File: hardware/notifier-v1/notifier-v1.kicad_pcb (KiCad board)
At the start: 4 copper layers, 50 x 36 mm, 42 parts, among them J1 USB-C PWR/DATA, J2 GC9A01 DISPLAY, SW1 RESET, SW2 BOOT, SW3 BUTTON, U1 ESP32-S3-WROOM-1-N8R2, U2 USBLC6-2SC6, U3 TLV62569, U4 BME688, U5 SHT40-AD1B

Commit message: notifier-v1: USB 22 ohm series resistors, 1 uF at module 3V3, second buck output cap
Co-Authored-By: Claude Opus 5.5 <noreply@anthropic.com>
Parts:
- added C10: 1u, Capacitor_SMD:C_0402_1005Metric, F.Cu at (113.7, 110.6)
- added C11: 22u, Capacitor_SMD:C_0805_2012Metric, F.Cu at (130.2, 126.9)
- added R11: 22, Resistor_SMD:R_0402_1005Metric, F.Cu at (113.5, 116.5)
- added R12: 22, Resistor_SMD:R_0402_1005Metric, F.Cu at (113.5, 117.7)
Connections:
- U1 pad 13: /USB_DN -> /MCU/USB_DN_MCU
- U1 pad 14: /USB_DP -> /MCU/USB_DP_MCU
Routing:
- net /USB_DN: track 16.8 -> 32.9 mm, vias 2 -> 0
- net GND: track 178.0 -> 189.8 mm, vias 15 -> 18
- net /MCU/BTN: track 50.2 -> 42.8 mm, vias 9 -> 4
- net /MCU/BOOT: track 63.9 -> 69.6 mm, vias 4 -> 5
- net /MCU/USB_DN_MCU: track 0.00 -> 5.29 mm, vias 0 -> 2
- net /MCU/USB_DP_MCU: track 0.00 -> 3.89 mm, vias 0 -> 2
- net /I2C_SCL: track 46.2 -> 48.4 mm, vias 5 -> 7
- net +3V3: track 145.5 -> 147.2 mm, vias 4 -> 2
- net /I2C_SDA: track 46.9 -> 48.2 mm
- net /USB_DP: track 17.2 -> 18.2 mm, vias 3 -> 2
- net /Power/LED_A: track 3.75 -> 4.67 mm
- net /MCU/RXD0: track 6.37 -> 5.67 mm
- net VBUS: track 27.7 -> 27.0 mm
- net VBUS_IN: track 20.5 -> 20.7 mm, vias 3 -> 5

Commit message: notifier-v1: 90 ohm USB pair, hand-drawn and locked
USB D+/D- are 0.27 mm with a 0.15 mm gap on F.Cu over the In1 GND plane: 90 ohm
differential on JLC04161H-7628 (prepreg 0.2104 mm, er 4.4, 1 oz, solder mask).
The router left the pair partial (interleaved USB-C pads) and snaked it over
B.Cu with ~8 vias; drawing it in layout_v1.py makes it straight, via-free and
the pipeline passed 4 of 4 runs (was ~1 of 3).

- U2 (USBLC6) rotated 270 for flow-through; VBUS_IN/GND middle pins by via
- module-side nets renamed MCU_USB_DP/MCU_USB_DN (KRT pairs by suffix)
- route_krt.sh: diff stage dropped, --keep-input-copper
- ORDER.md: calculator inputs to verify; hw-layout skill updated

Co-Authored-By: Claude Opus 5.5 <noreply@anthropic.com>
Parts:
- moved U2 0.50 mm to (115.0, 124.0), turned to -90 degrees
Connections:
- net /MCU/USB_DN_MCU renamed /MCU/MCU_USB_DN
- net /MCU/USB_DP_MCU renamed /MCU/MCU_USB_DP
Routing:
- net /MCU/BTN: track 42.8 -> 63.5 mm
- net /USB_DN: track 32.9 -> 16.2 mm
- net /MCU/BOOT: track 69.6 -> 84.9 mm, vias 5 -> 3
- net /Power/CC1: track 6.56 -> 18.0 mm
- net +3V3: track 147.2 -> 158.6 mm, vias 2 -> 8
- net /I2C_SCL: track 48.4 -> 55.1 mm, vias 7 -> 6
- net /USB_DP: track 18.2 -> 14.4 mm, vias 2 -> 0
- net /MCU/MCU_USB_DN: track 5.29 -> 2.36 mm, vias 2 -> 0
- net /MCU/EN: track 63.3 -> 65.9 mm, vias 5 -> 3
- net /MCU/MCU_USB_DP: track 3.89 -> 2.36 mm, vias 2 -> 0
- net VBUS_IN: track 20.7 -> 19.8 mm
- net /I2C_SDA: track 48.2 -> 47.5 mm
- net /Power/CC2: track 6.26 -> 6.70 mm, vias 0 -> 2
- net GND: track 189.8 -> 190.0 mm, vias 18 -> 17

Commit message: hardware: save schematics in the KiCad 10 format; skill lessons
build_v1.sh runs `kicad-cli sch upgrade --force` on every sheet (the
generator writes the 9.0 header; KiCad 10.0.7 warned on open). Skills: file
format and diff-pair naming (hw-schematic), hand-drawn locked nets and pair
checks (hw-layout), impedance calculator workflow (hw-bom).

Co-Authored-By: Claude Opus 5.5 <noreply@anthropic.com>
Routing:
- net /I2C_SCL: track 55.1 -> 49.8 mm, vias 6 -> 7
- net /LCD_SCLK: track 15.8 -> 19.5 mm, vias 0 -> 2
- net /LCD_MOSI: track 18.9 -> 22.1 mm, vias 1 -> 2
- net /I2C_SDA: track 47.5 -> 50.6 mm
- net +3V3: track 158.6 -> 161.3 mm, vias 8 -> 10
- net /LCD_RST: track 18.4 -> 16.3 mm, vias 0 -> 2
- net GND: track 190.0 -> 188.3 mm
- net VBUS_IN: track 19.8 -> 18.4 mm
- net /LCD_DC: track 20.5 -> 21.6 mm, vias 1 -> 0
- net /LCD_CS: track 20.3 -> 21.1 mm, vias 3 -> 0
- net /Display/LCD_VCC: track 4.25 -> 4.96 mm
- net /MCU/RXD0: track 5.67 -> 6.37 mm

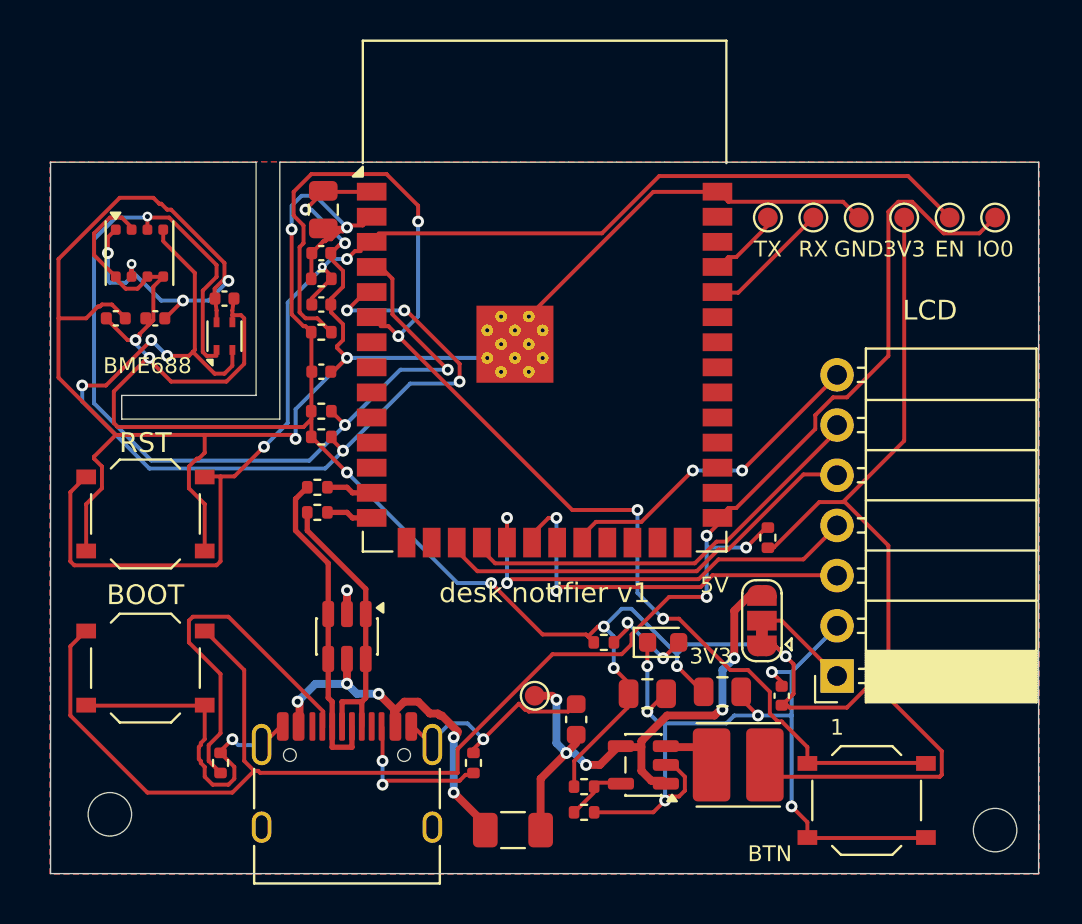
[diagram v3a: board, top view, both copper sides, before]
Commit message: Sensor neck: no plane under island/neck, guarded 0.15 mm bus, wider slot
- In1 GND left out under the sensor island and neck; the neck bus is
  3V3 | GND | SDA | SCL | GND at 0.15 mm, guards joined on B.Cu and
  stitched to In1 below the neck
- Module-side slot widened to 1.8 mm (island side stays 1.2 mm)
- Island hand-routed and locked (deterministic, clear of SHT40 keepout)
- C12 4.7u bulk cap where 3V3 enters the island
- R13 33R in series with LCD_SCLK (new net MCU_LCD_SCLK), GND vias
  beside the SPI layer changes where there is room
- In2 island removal drops slivers between the module thermal vias

Co-Authored-By: Claude Opus 5.5 <noreply@anthropic.com>
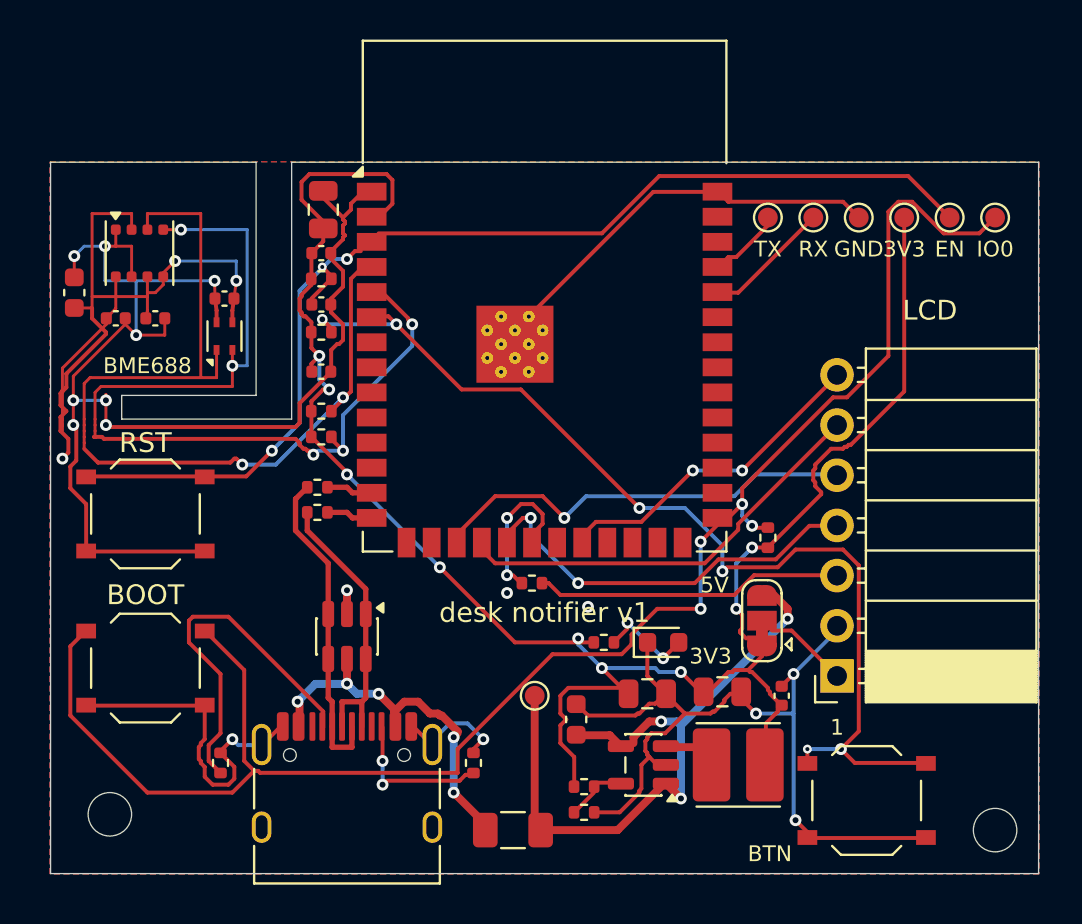
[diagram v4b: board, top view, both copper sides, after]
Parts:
- added C12: 4.7u, Capacitor_SMD:C_0603_1608Metric, F.Cu at (101.2, 106.6)
- added R13: 33, Resistor_SMD:R_0402_1005Metric, F.Cu at (124.4, 121.3)
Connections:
- U1 pad 20: /LCD_SCLK -> /MCU/MCU_LCD_SCLK
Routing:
- net GND: track 188.3 -> 160.8 mm, vias 17 -> 16
- net +3V3: track 161.3 -> 137.8 mm, vias 10 -> 12
- net /MCU/BTN: track 63.1 -> 52.3 mm, vias 4 -> 6
- net /MCU/EN: track 65.9 -> 55.6 mm
- net /MCU/MCU_LCD_SCLK: track 0.00 -> 6.97 mm, vias 0 -> 2
- net VBUS: track 27.0 -> 33.4 mm, vias 5 -> 3
- net /I2C_SDA: track 50.6 -> 46.3 mm, vias 3 -> 2
- net /LCD_SCLK: track 19.5 -> 15.6 mm, vias 2 -> 0
- net /I2C_SCL: track 49.8 -> 46.3 mm, vias 7 -> 5
- net /LCD_MOSI: track 22.1 -> 20.1 mm
- net /MCU/BOOT: track 85.4 -> 83.8 mm, vias 3 -> 4
- net /Display/LCD_VCC: track 4.96 -> 4.25 mm
- net /LCD_DC: track 21.6 -> 21.4 mm, vias 0 -> 1
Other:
- outline, holes or cut-outs redrawn

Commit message: Layout A: USB-C on the back edge, corner mounts, no buttons, JLC fab data
- J2 display socket mirrored (1 RST 2 CS 3 DC 4 SDA 5 SCL 6 GND 7 VCC),
  face at the right edge
- USB-C J1 on the left edge (enclosure back), ESD/CC/fuse beside it,
  hand-drawn 0.27/0.15 pair (~91 ohm diff, tools/impedance.py), only
  GND under the shell (DRC rule area)
- SW1-SW3/R6/BTN removed; 1.5 mm debug pads TX RX 3V3 EN GND IO0;
  firmware DESK_BTN = -1 on notifier-v1
- Four M2 corner holes with keepouts; sensor island grown to 14.8 mm
  with H3 in its corner, re-hand-routed (BME688/SHT40 8.9 mm apart)
- I2C >= 1.6 mm from USB on the same layer; vias >= 0.15 mm from
  same-net SMD pads (rule), hand vias >= 0.2 mm
- Silk "v1 ${GIT_SHA}" resolved at fab export; JLC order-number mark
- Fab: Protel gerbers without X2, PTH/NPTH split, JLC BOM/CPL, CPL
  rotation fixes (U4 +90, U5 +270); pipeline --fab-only on a clean
  commit; route retry until the gate passes
- ORDER.md: stackup JLC04161H-7628, rails left/right, preview checklist,
  bring-up without buttons; PLAN.md enclosure notes

Co-Authored-By: Claude Opus 5.5 <noreply@anthropic.com>
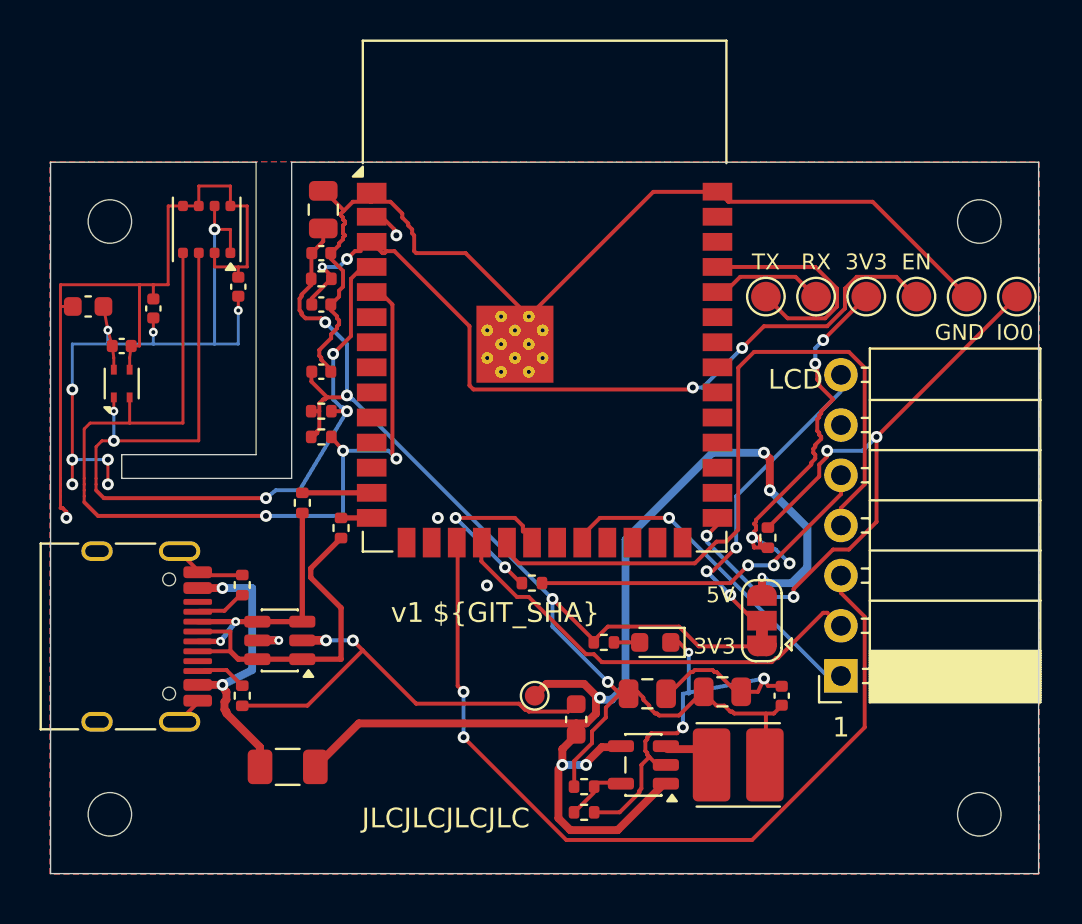
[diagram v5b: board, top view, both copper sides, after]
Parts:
- removed R6: 10k, Resistor_SMD:R_0402_1005Metric
- removed SW1: RESET, Button_Switch_SMD:SW_Push_1P1T_XKB_TS-1187A
- removed SW2: BOOT, Button_Switch_SMD:SW_Push_1P1T_XKB_TS-1187A
- removed SW3: BUTTON, Button_Switch_SMD:SW_Push_1P1T_XKB_TS-1187A
- added H3: M2, MountingHole:MountingHole_2.2mm_M2, F.Cu at (103.0, 103.0)
- added H4: M2, MountingHole:MountingHole_2.2mm_M2, F.Cu at (147.0, 103.0)
- TP1, TP2, TP3, TP4, TP5, TP6: footprint TestPoint:TestPoint_Pad_D1.0mm -> TestPoint:TestPoint_Pad_D1.5mm
- moved J1 14.4 mm to (103.4, 124.0), turned to -90 degrees
- moved R2 12.2 mm to (109.7, 127.0), turned to -90 degrees
- moved F1 11.8 mm to (112.0, 130.6)
- moved R1 9.07 mm to (109.7, 121.4)
- moved TP3 6.77 mm to (146.4, 106.8)
- moved U5 5.73 mm to (103.6, 111.2)
- moved C9 5.73 mm to (103.6, 109.3)
- moved C8 4.49 mm to (109.5, 106.3), turned to -90 degrees
- moved TP4 4.44 mm to (141.3, 106.8)
- moved TP5 4.34 mm to (143.8, 106.8)
- moved TP6 4.15 mm to (148.9, 106.8)
- moved TP2 4.00 mm to (138.7, 106.8)
- moved TP1 4.00 mm to (136.2, 106.8)
- moved U4 3.61 mm to (107.9, 103.4), turned to 180 degrees
- moved U2 3.41 mm to (111.6, 124.2), turned to 180 degrees
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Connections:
- J2 pad 1: /Display/LCD_VCC -> /LCD_RST
- J2 pad 2: GND -> /LCD_CS
- J2 pad 3: /LCD_SCLK -> /LCD_DC
- J2 pad 5: /LCD_DC -> /LCD_SCLK
- J2 pad 6: /LCD_CS -> GND
- J2 pad 7: /LCD_RST -> /Display/LCD_VCC
- U1 pad 6: /MCU/BTN -> unconnected-(U1-IO6-Pad6)
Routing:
- net /MCU/BTN: track 52.3 -> 0.00 mm, vias 6 -> 0
- net /MCU/BOOT: track 83.8 -> 34.4 mm
- net VBUS: track 33.4 -> 62.8 mm, vias 3 -> 6
- net /LCD_DC: track 21.4 -> 43.0 mm, vias 1 -> 2
- net GND: track 160.8 -> 141.9 mm
- net /LCD_MOSI: track 20.1 -> 36.4 mm, vias 2 -> 0
- net /Power/CC1: track 18.5 -> 2.43 mm
- net /MCU/EN: track 55.6 -> 40.0 mm, vias 3 -> 4
- net /Display/LCD_VCC: track 4.25 -> 15.2 mm, vias 0 -> 3
- net +3V3: track 137.8 -> 129.0 mm, vias 12 -> 10
- net /MCU/TXD0: track 3.37 -> 11.7 mm
- net /Power/CC2: track 7.12 -> 2.23 mm, vias 2 -> 0
- net /Power/LED_A: track 4.67 -> 1.31 mm, vias 2 -> 0
- net /USB_DP: track 14.4 -> 17.5 mm
- net /I2C_SDA: track 46.3 -> 43.3 mm, vias 2 -> 5
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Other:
- outline, holes or cut-outs redrawn
- board text added: "JLCJLCJLCJLC"
- board text added: "v1 ${GIT_SHA}"
- board text removed: "BME688"
- board text removed: "BOOT"
- board text removed: "BTN"
- board text removed: "desk notifier v1"
